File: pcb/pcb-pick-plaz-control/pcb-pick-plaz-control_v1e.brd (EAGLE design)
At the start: 100 x 100 mm, 202 parts, among them J1 USB-ID-THT, J3 USB-LCSC_C42431, J3C USB-LCSC_C42431, J3C1 USB-LCSC_C42431, U1 STM32F411VET6, U2 CH340, U3 TPS54227DDAR, U4 SL2.1A, U5 TPS54227DDAR, X1 04-JST-B4B-XH-A, X10 03-JST-B3B-XH-A, X11 03-JST-B3B-XH-A, X12 03-JST-B3B-XH-A, X13 02-JST-B3B-XH-A, X14 02-JST-B3B-XH-A, X15 02-JST-B3B-XH-A, X16 02-JST-B3B-XH-A, X17 02-JST-B3B-XH-A, X18 02-JST-B3B-XH-A, X19 05-JST-B5B-XH-A, X2 04-JST-B4B-XH-A, X20 05-JST-B5B-XH-A, X21 04-JST-B4B-XH-A, X22 PIN_2X13.81MM_LONGPAD, X23 02-JST-B3B-XH-A, X24 02-JST-B3B-XH-A, X25 04-JST-B4B-XH-A, X26 05-JST-B5B-XH-A, X27 05-JST-B5B-XH-A, X28 05-JST-B5B-XH-A, X29 02-JST-B3B-XH-A, X3 04-JST-B4B-XH-A, X30 02-JST-B3B-XH-A, X31 02-JST-B3B-XH-A, X32 02-JST-B3B-XH-A, X33 04-JST-B4B-XH-A, X4 04-JST-B4B-XH-A, X5 04-JST-B4B-XH-A, X6 04-JST-B4B-XH-A, X7 03-JST-B3B-XH-A, X8 03-JST-B3B-XH-A, X9 03-JST-B3B-XH-A, Y1 3213-QUARZ3225, Y2 3213-QUARZ3225, Y3 3213-QUARZ3225

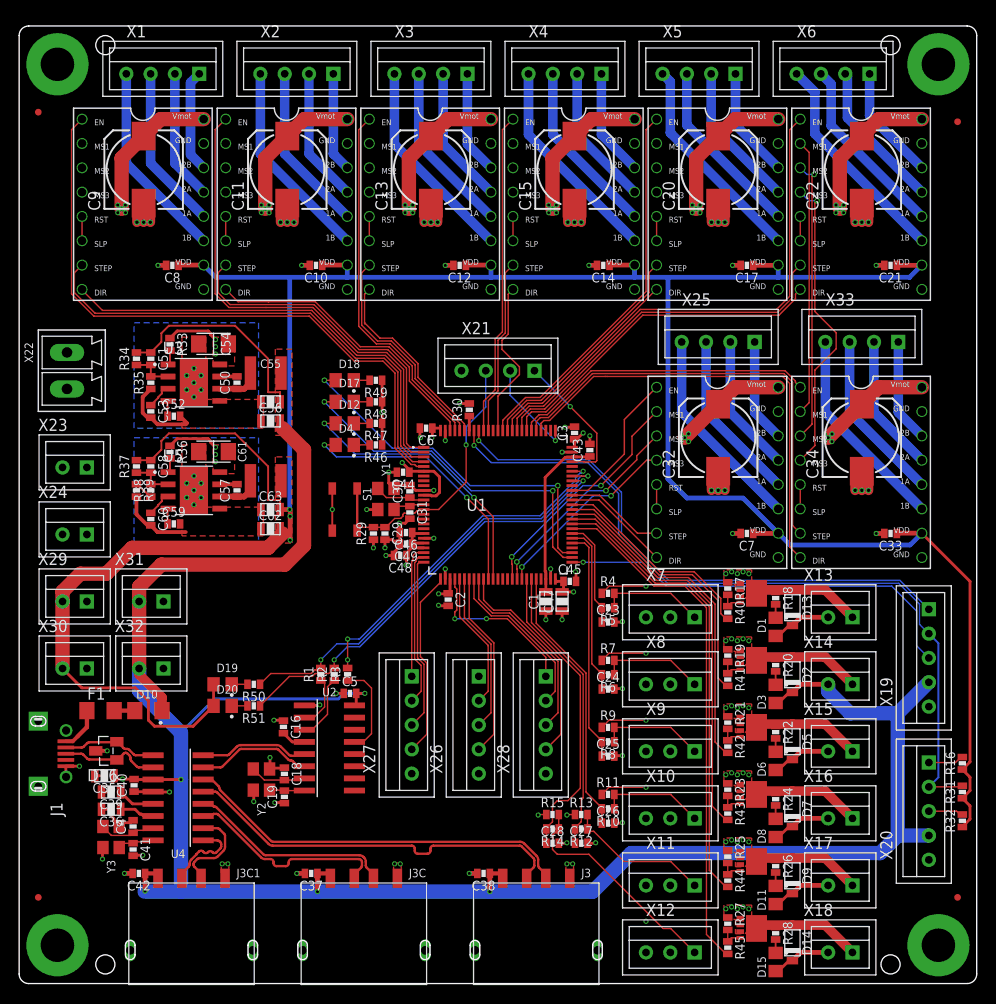
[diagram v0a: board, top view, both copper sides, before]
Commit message: updated pcbs with step files
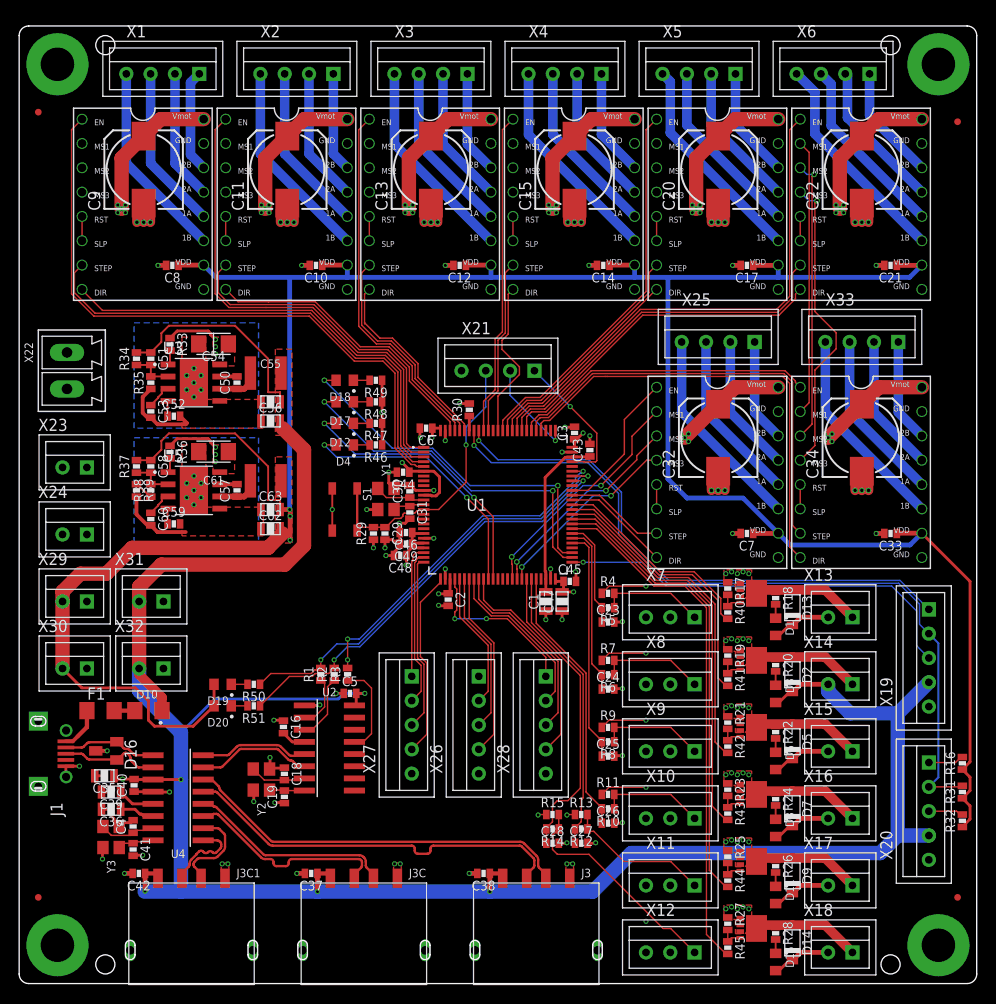
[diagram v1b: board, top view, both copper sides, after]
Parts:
- turned C54 to 180 degrees
- turned C61 to 180 degrees
- turned D1 to 270 degrees
- turned D11 to 270 degrees
- turned D12 to 180 degrees
- turned D15 to 270 degrees
- turned D16 to 90 degrees
- turned D17 to 180 degrees
- turned D18 to 180 degrees
- turned D19 to 180 degrees
- turned D20 to 180 degrees
- turned D3 to 270 degrees
- turned D4 to 180 degrees
- turned D6 to 270 degrees
- turned D8 to 270 degrees
